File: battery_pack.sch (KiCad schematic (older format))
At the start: 6 parts

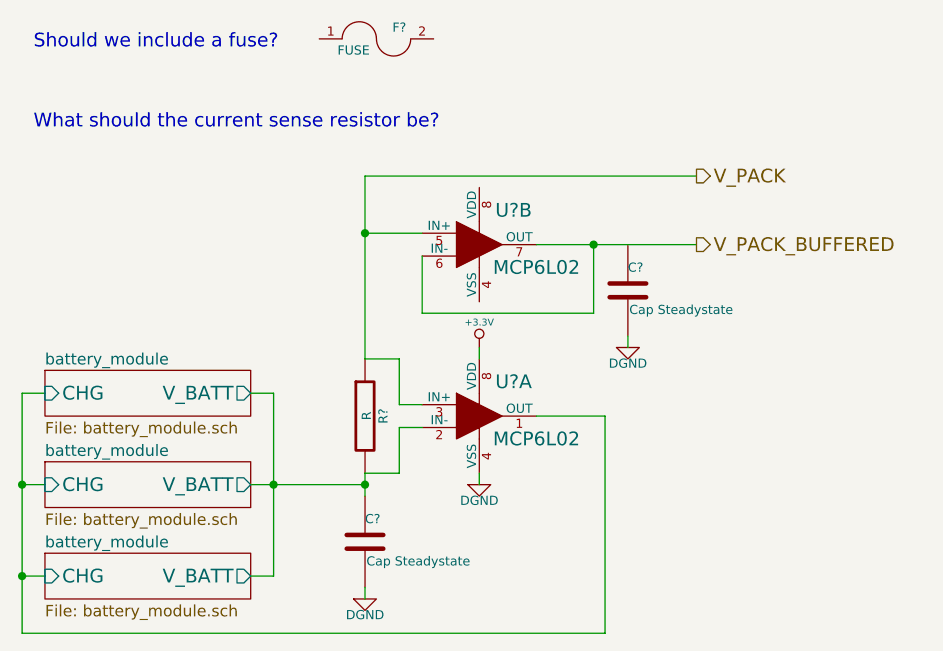
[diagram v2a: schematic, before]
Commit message: various fixes due to issues found in ERC
learned how to use invisible pins
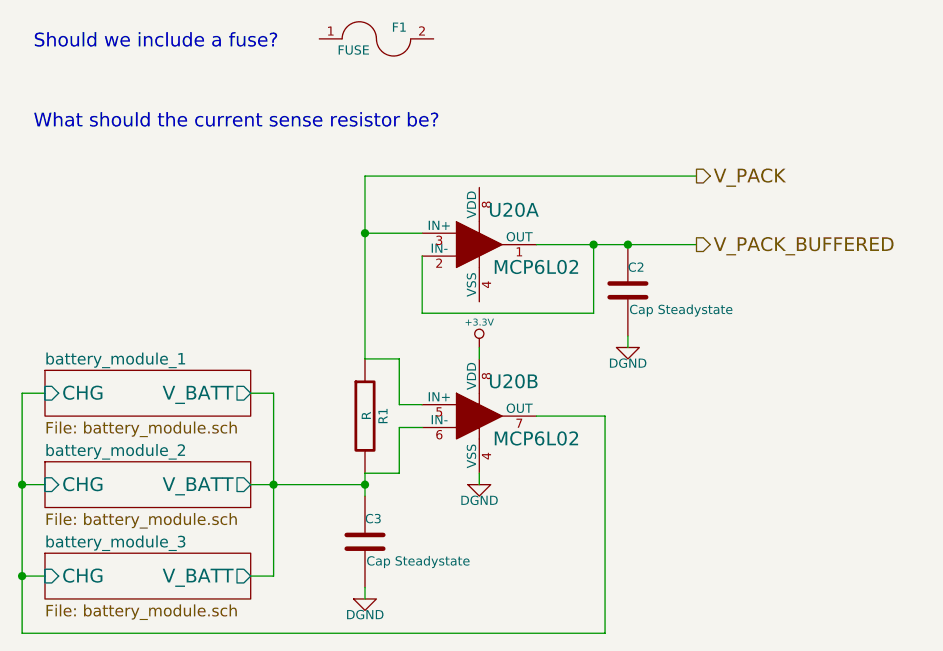
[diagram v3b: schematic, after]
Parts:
- gave numbers to parts that had none: 5
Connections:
- net V_PACK: now also U20.3 (IN+), U20.5 (IN+); no longer U20.3 (IN+), U20.5 (IN+)
- net V_PACK_BUFFERED: now also C2.1, U20.1 (OUT), U20.2 (IN-); no longer U20.6 (IN-), U20.7 (OUT)
- removed net battery_module/CHG: U20.1 (OUT)
- net battery_module/V_BATT renamed battery_module_1/V_BATT
- net battery_module_1/V_BATT: now also U20.6 (IN-); no longer U20.2 (IN-)
- new net battery_module_1/CHG: U20.7 (OUT)
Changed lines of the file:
@@
 Sheet 2 18
 Title ""
-Date "18 dec 2013"
+Date "20 dec 2013"
 Rev ""
 Comp ""
@@
 S 700  2100 900  200
 U 5281D330
-F0 "battery_module" 50
+F0 "battery_module_1" 50
 F1 "battery_module.sch" 50
 F2 "V_BATT" O R 1600 2200 60
@@
 S 700  2500 900  200
 U 5281E180
-F0 "battery_module" 50
+F0 "battery_module_2" 50
 F1 "battery_module.sch" 50
 F2 "V_BATT" O R 1600 2600 60
@@
 S 700  2900 900  200
 U 5281E2A4
-F0 "battery_module" 50
+F0 "battery_module_3" 50
 F1 "battery_module.sch" 50
 F2 "V_BATT" O R 1600 3000 60
@@
 	1600 2200 1700 2200
 Wire Wire Line
-	1700 2200 1700 2600
-Wire Wire Line
-	1700 2600 1700 3000
-Wire Wire Line
-	1600 2600 1700 2600
-Wire Wire Line
-	1700 2600 2100 2600
+	1700 2200 1700 3000
+Wire Wire Line
+	1600 2600 2100 2600
 Wire Wire Line
 	1700 3000 1600 3000
 Connection ~ 1700 2600
 $Comp
-L C C?
+L C C3
 U 1 1 5281E7DA
 P 2100 2850
-F 0 "C?" H 2100 2950 40  0000 L CNN
+F 0 "C3" H 2100 2950 40  0000 L CNN
 F 1 "Cap Steadystate" H 2106 2765 40  0000 L CNN
 F 2 "~" H 2138 2700 30  0000 C CNN
@@
 $EndComp
 $Comp
-L DGND #PWR?
+L DGND #PWR04
 U 1 1 5281E7E0
 P 2100 3100
-F 0 "#PWR?" H 2100 3100 40  0001 C CNN
+F 0 "#PWR04" H 2100 3100 40  0001 C CNN
 F 1 "DGND" H 2100 3030 40  0000 C CNN
 F 2 "" H 2100 3100 60  0000 C CNN
@@
 	2100 3050 2100 3100
 Wire Wire Line
-	2100 2550 2100 2600
-Wire Wire Line
-	2100 2600 2100 2650
-$Comp
-L R R?
+	2100 2550 2100 2650
+$Comp
+L R R1
 U 1 1 5281E89A
 P 2100 2300
-F 0 "R?" V 2180 2300 40  0000 C CNN
+F 0 "R1" V 2180 2300 40  0000 C CNN
 F 1 "R" V 2107 2301 40  0000 C CNN
 F 2 "~" V 2030 2300 30  0000 C CNN
@@
 Connection ~ 2100 2600
 Wire Wire Line
-	2100 1250 2100 1500
-Wire Wire Line
-	2100 1500 2100 2050
+	2100 1250 2100 2050
 Wire Wire Line
 	2100 2050 2250 2050
@@
 	2250 2350 2350 2350
 $Comp
-L FUSE F?
+L FUSE F1
 U 1 1 5281EB5E
 P 2150 650
-F 0 "F?" H 2250 700 40  0000 C CNN
+F 0 "F1" H 2250 700 40  0000 C CNN
 F 1 "FUSE" H 2050 600 40  0000 C CNN
 F 2 "~" H 2150 650 60  0000 C CNN
@@
 $EndComp
 $Comp
-L MCP6L02 U?
-U 1 1 5281F116
+L MCP6L02 U20
+U 2 1 5281F116
 P 2600 2300
-F 0 "U?" H 2750 2450 60  0000 C CNN
+F 0 "U20" H 2750 2450 60  0000 C CNN
 F 1 "MCP6L02" H 2850 2200 60  0000 C CNN
 F 2 "" H 2600 2300 60  0000 C CNN
 F 3 "" H 2600 2300 60  0000 C CNN
-	1    2600 2300
-	1    0    0    -1
-$EndComp
-$Comp
-L DGND #PWR?
+	2    2600 2300
+	1    0    0    -1
+$EndComp
+$Comp
+L DGND #PWR05
 U 1 1 5281F123
 P 2600 2600
-F 0 "#PWR?" H 2600 2600 40  0001 C CNN
+F 0 "#PWR05" H 2600 2600 40  0001 C CNN
 F 1 "DGND" H 2600 2530 40  0000 C CNN
 F 2 "" H 2600 2600 60  0000 C CNN
@@
 	2600 2550 2600 2600
 $Comp
-L +3.3V #PWR?
+L +3.3V #PWR06
 U 1 1 5281F172
 P 2600 2000
-F 0 "#PWR?" H 2600 1960 30  0001 C CNN
+F 0 "#PWR06" H 2600 1960 30  0001 C CNN
 F 1 "+3.3V" H 2600 2110 30  0000 C CNN
 F 2 "" H 2600 2000 60  0000 C CNN
@@
 	700  2200 600  2200
 Wire Wire Line
-	600  2200 600  2600
-Wire Wire Line
-	600  2600 600  3000
-Wire Wire Line
-	600  3000 600  3250
+	600  2200 600  3250
 Wire Wire Line
 	600  2600 700  2600
@@
 V_PACK_BUFFERED
 $Comp
-L MCP6L02 U?
-U 2 1 5281F4C0
+L MCP6L02 U20
+U 1 1 5281F4C0
 P 2600 1550
-F 0 "U?" H 2750 1700 60  0000 C CNN
+F 0 "U20" H 2750 1700 60  0000 C CNN
 F 1 "MCP6L02" H 2850 1450 60  0000 C CNN
 F 2 "" H 2600 1550 60  0000 C CNN
 F 3 "" H 2600 1550 60  0000 C CNN
-	2    2600 1550
+	1    2600 1550
 	1    0    0    -1
 $EndComp
@@
 	3100 1850 3100 1550
 Wire Wire Line
-	2850 1550 3100 1550
-Wire Wire Line
-	3100 1550 3550 1550
+	2850 1550 3550 1550
 Wire Wire Line
 	2100 1500 2350 1500
@@
 Connection ~ 2100 1500
 $Comp
-L C C?
+L C C2
 U 1 1 5281F708
 P 3250 1750
-F 0 "C?" H 3250 1850 40  0000 L CNN
+F 0 "C2" H 3250 1850 40  0000 L CNN
 F 1 "Cap Steadystate" H 3256 1665 40  0000 L CNN
 F 2 "~" H 3288 1600 30  0000 C CNN
@@
 $EndComp
 $Comp
-L DGND #PWR?
+L DGND #PWR07
 U 1 1 5281F70E
 P 3250 2000
-F 0 "#PWR?" H 3250 2000 40  0001 C CNN
+F 0 "#PWR07" H 3250 2000 40  0001 C CNN
 F 1 "DGND" H 3250 1930 40  0000 C CNN
 F 2 "" H 3250 2000 60  0000 C CNN
@@
 Text Notes 650  1050 0    60   ~ 0
 What should the current sense resistor be?
+Connection ~ 3250 1550
 $EndSCHEMATC

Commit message: placed components ... quite the task!
there is a lot of shit going on in this board... :D
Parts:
- removed F1: FUSE, ~, symbol FUSE
- renumbered C2 to C1, C3 to C2
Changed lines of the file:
@@
 $Descr A4 11693 8268
 encoding utf-8
-Sheet 2 18
+Sheet 2 15
 Title ""
-Date "12 jan 2014"
+Date "18 jan 2014"
 Rev ""
 Comp ""
@@
 Connection ~ 1700 2600
 $Comp
-L C C3
+L C C2
 U 1 1 5281E7DA
 P 2100 2850
-F 0 "C3" H 2100 2950 40  0000 L CNN
+F 0 "C2" H 2100 2950 40  0000 L CNN
 F 1 "Cap Steadystate" H 2106 2765 40  0000 L CNN
 F 2 "~" H 2138 2700 30  0000 C CNN
@@
 $EndComp
 $Comp
-L DGND #PWR04
+L DGND #PWR02
 U 1 1 5281E7E0
 P 2100 3100
-F 0 "#PWR04" H 2100 3100 40  0001 C CNN
+F 0 "#PWR02" H 2100 3100 40  0001 C CNN
 F 1 "DGND" H 2100 3030 40  0000 C CNN
 F 2 "" H 2100 3100 60  0000 C CNN
@@
 	2250 2350 2350 2350
 $Comp
-L FUSE F1
+L FUSE #F1
 U 1 1 5281EB5E
 P 2150 650
-F 0 "F1" H 2250 700 40  0000 C CNN
+F 0 "#F1" H 2250 700 40  0000 C CNN
 F 1 "FUSE" H 2050 600 40  0000 C CNN
 F 2 "~" H 2150 650 60  0000 C CNN
@@
 $EndComp
 $Comp
-L DGND #PWR05
+L DGND #PWR03
 U 1 1 5281F123
 P 2600 2600
-F 0 "#PWR05" H 2600 2600 40  0001 C CNN
+F 0 "#PWR03" H 2600 2600 40  0001 C CNN
 F 1 "DGND" H 2600 2530 40  0000 C CNN
 F 2 "" H 2600 2600 60  0000 C CNN
@@
 	2600 2550 2600 2600
 $Comp
-L +3.3V #PWR06
+L +3.3V #PWR04
 U 1 1 5281F172
 P 2600 2000
-F 0 "#PWR06" H 2600 1960 30  0001 C CNN
+F 0 "#PWR04" H 2600 1960 30  0001 C CNN
 F 1 "+3.3V" H 2600 2110 30  0000 C CNN
 F 2 "" H 2600 2000 60  0000 C CNN
@@
 Connection ~ 2100 1500
 $Comp
-L C C2
+L C C1
 U 1 1 5281F708
 P 3250 1750
-F 0 "C2" H 3250 1850 40  0000 L CNN
+F 0 "C1" H 3250 1850 40  0000 L CNN
 F 1 "Cap Steadystate" H 3256 1665 40  0000 L CNN
 F 2 "~" H 3288 1600 30  0000 C CNN
@@
 $EndComp
 $Comp
-L DGND #PWR07
+L DGND #PWR05
 U 1 1 5281F70E
 P 3250 2000
-F 0 "#PWR07" H 3250 2000 40  0001 C CNN
+F 0 "#PWR05" H 3250 2000 40  0001 C CNN
 F 1 "DGND" H 3250 1930 40  0000 C CNN
 F 2 "" H 3250 2000 60  0000 C CNN

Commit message: revisions to board and sch
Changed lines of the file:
@@
 $Descr A4 11693 8268
 encoding utf-8
-Sheet 2 15
+Sheet 2 16
 Title ""
-Date "18 jan 2014"
+Date "1 feb 2014"
 Rev ""
 Comp ""
@@
 F3 "CHG" I L 700 2200 60
 $EndSheet
-$Sheet
-S 700  2500 900  200
-U 5281E180
-F0 "battery_module_2" 50
-F1 "battery_module.sch" 50
-F2 "V_BATT" O R 1600 2600 60
-F3 "CHG" I L 700 2600 60
-$EndSheet
-$Sheet
-S 700  2900 900  200
-U 5281E2A4
-F0 "battery_module_3" 50
-F1 "battery_module.sch" 50
-F2 "V_BATT" O R 1600 3000 60
-F3 "CHG" I L 700 3000 60
-$EndSheet
 Text HLabel 3550 1250 2    60   Output ~ 0
 V_PACK
@@
 U 1 1 5281EB5E
 P 2150 650
-F 0 "#F1" H 2250 700 40  0000 C CNN
+F 0 "#F1" H 2250 700 40  0001 C CNN
 F 1 "FUSE" H 2050 600 40  0000 C CNN
 F 2 "~" H 2150 650 60  0000 C CNN
@@
 	600  2200 600  3250
 Wire Wire Line
-	600  2600 700  2600
-Wire Wire Line
 	600  3000 700  3000
 Connection ~ 600  2600
@@
 What should the current sense resistor be?
 Connection ~ 3250 1550
+Wire Wire Line
+	600  2600 700  2600
 $EndSCHEMATC
